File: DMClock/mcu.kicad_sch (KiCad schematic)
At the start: 0 parts

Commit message: adding mplabxide init files
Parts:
- added U1: PIC16F877A-I_P, Footprints:DIP254P1524X483-40, symbol PIC16F877A-I_P:PIC16F877A-I_P
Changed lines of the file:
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@@
 (kicad_sch (version 20230121) (generator eeschema)
   (paper "A4")
+  (symbol (lib_id "PIC16F877A-I_P:PIC16F877A-I_P") (at 136.652 90.678 0) (unit 1)
+    (in_bom yes) (on_board yes) (dnp no) (fields_autoplaced)
+    (property "Reference" "U1" (at 136.652 52.705 0)
+      (effects (font (size 1.27 1.27)))
+    )
+    (property "Value" "PIC16F877A-I_P" (at 136.652 55.245 0)
+      (effects (font (size 1.27 1.27)))
+    )
+    (property "Footprint" "Footprints:DIP254P1524X483-40" (at 136.652 90.678 0)
+      (effects (font (size 1.27 1.27)) (justify bottom) hide)
+    )
+    (property "Datasheet" "" (at 136.652 90.678 0)
+      (effects (font (size 1.27 1.27)) hide)
+    )
+    (property "MF" "Microchip" (at 136.652 90.678 0)
+      (effects (font (size 1.27 1.27)) (justify bottom) hide)
+    )
+    (property "Description" "\nMicrocontroller, 8bit PIC, 20MHz, 14.3kb, 256 B Flash, 40-Pin PDIP | Microchip Technology Inc. PIC16F877A-I/P\n" (at 136.652 90.678 0)
+      (effects (font (size 1.27 1.27)) (justify bottom) hide)
+    )
+    (property "PACKAGE" "DIP-40" (at 136.652 90.678 0)
+      (effects (font (size 1.27 1.27)) (justify bottom) hide)
+    )
+    (property "MPN" "PIC16F877A-I/P" (at 136.652 90.678 0)
+      (effects (font (size 1.27 1.27)) (justify bottom) hide)
+    )
+    (property "Price" "None" (at 136.652 90.678 0)
+      (effects (font (size 1.27 1.27)) (justify bottom) hide)
+    )
+    (property "Package" "DIP-40 Microchip" (at 136.652 90.678 0)
+      (effects (font (size 1.27 1.27)) (justify bottom) hide)
+    )
+    (property "OC_FARNELL" "9761446" (at 136.652 90.678 0)
+      (effects (font (size 1.27 1.27)) (justify bottom) hide)
+    )
+    (property "SnapEDA_Link" "https://www.snapeda.com/parts/PIC16F877A-I/P/Microchip/view-part/?ref=snap" (at 136.652 90.678 0)
+      (effects (font (size 1.27 1.27)) (justify bottom) hide)
+    )
+    (property "MP" "PIC16F877A-I/P" (at 136.652 90.678 0)
+      (effects (font (size 1.27 1.27)) (justify bottom) hide)
+    )
+    (property "SUPPLIER" "Microchip" (at 136.652 90.678 0)
+      (effects (font (size 1.27 1.27)) (justify bottom) hide)
+    )
+    (property "OC_NEWARK" "69K7640" (at 136.652 90.678 0)
+      (effects (font (size 1.27 1.27)) (justify bottom) hide)
+    )
+    (property "Availability" "In Stock" (at 136.652 90.678 0)
+      (effects (font (size 1.27 1.27)) (justify bottom) hide)
+    )
+    (property "Check_prices" "https://www.snapeda.com/parts/PIC16F877A-I/P/Microchip/view-part/?ref=eda" (at 136.652 90.678 0)
+      (effects (font (size 1.27 1.27)) (justify bottom) hide)
+    )
+    (pin "31")
+    (pin "20")
+    (pin "40")
+    (pin "5")
+    (pin "27")
+    (pin "33")
+    (pin "29")
+    (pin "14")
+    (pin "10")
+    (pin "28")
+    (pin "22")
+    (pin "21")
+    (pin "26")
+    (pin "3")
+    (pin "37")
+    (pin "12")
+    (pin "18")
+    (pin "1")
+    (pin "35")
+    (pin "39")
+    (pin "4")
+    (pin "6")
+    (pin "25")
+    (pin "38")
+    (pin "7")
+    (pin "19")
+    (pin "16")
+    (pin "8")
+    (pin "11")
+    (pin "32")
+    (pin "34")
+    (pin "15")
+    (pin "2")
+    (pin "24")
+    (pin "23")
+    (pin "36")
+    (pin "17")
+    (pin "9")
+    (pin "13")
+    (pin "30")
+    (instances
+      (project "DMClock"
+        (path "/b42b345f-a3f2-4eff-9109-2f4619119d33/8963f20e-1ea1-4ba0-ac82-90e49e093141"
+          (reference "U1") (unit 1)
+        )
+      )
+    )
+  )
 )

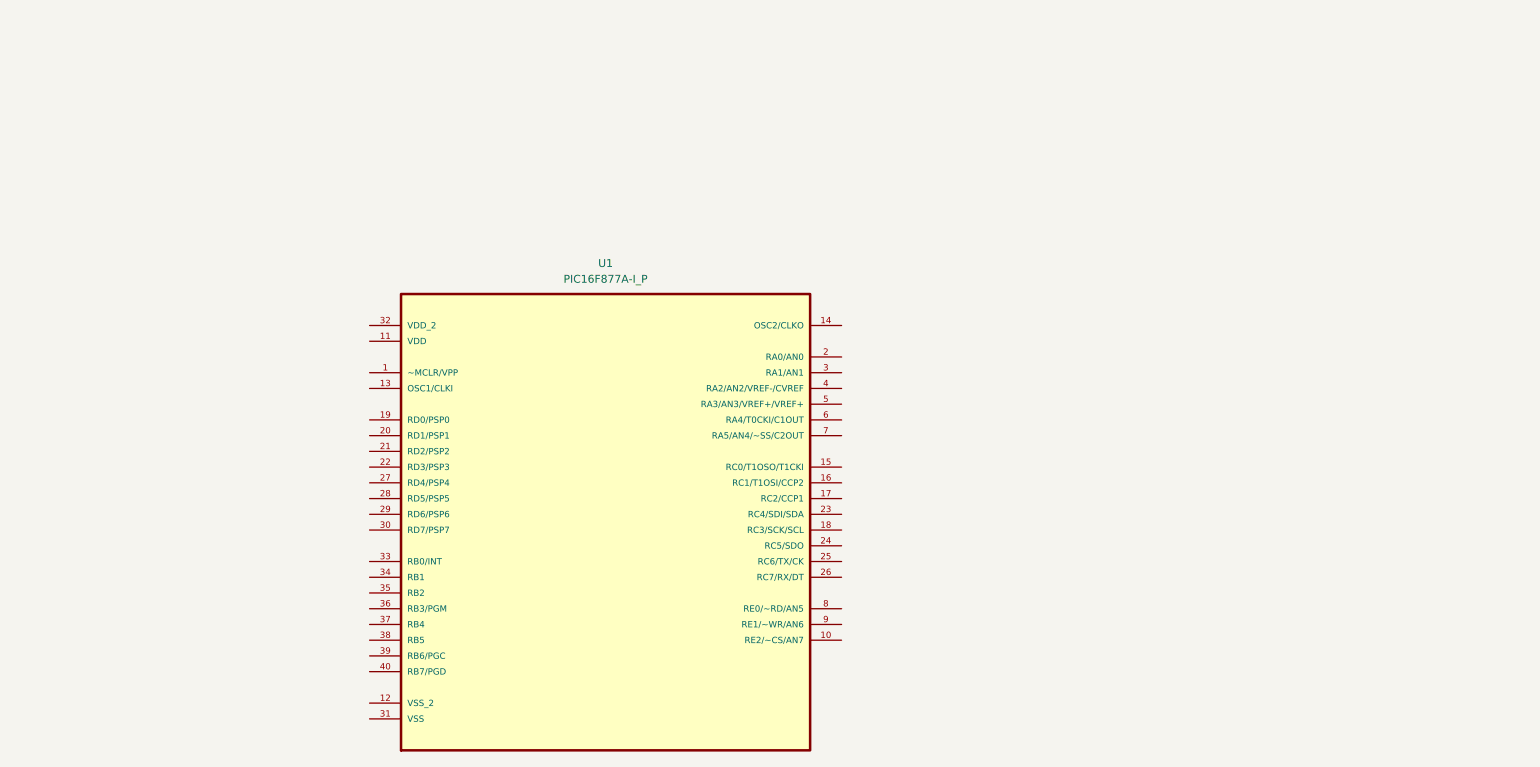
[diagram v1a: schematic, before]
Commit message: more modules added, still need to add a lot of footprints and see if there exist any sd card libraries for use with i2s
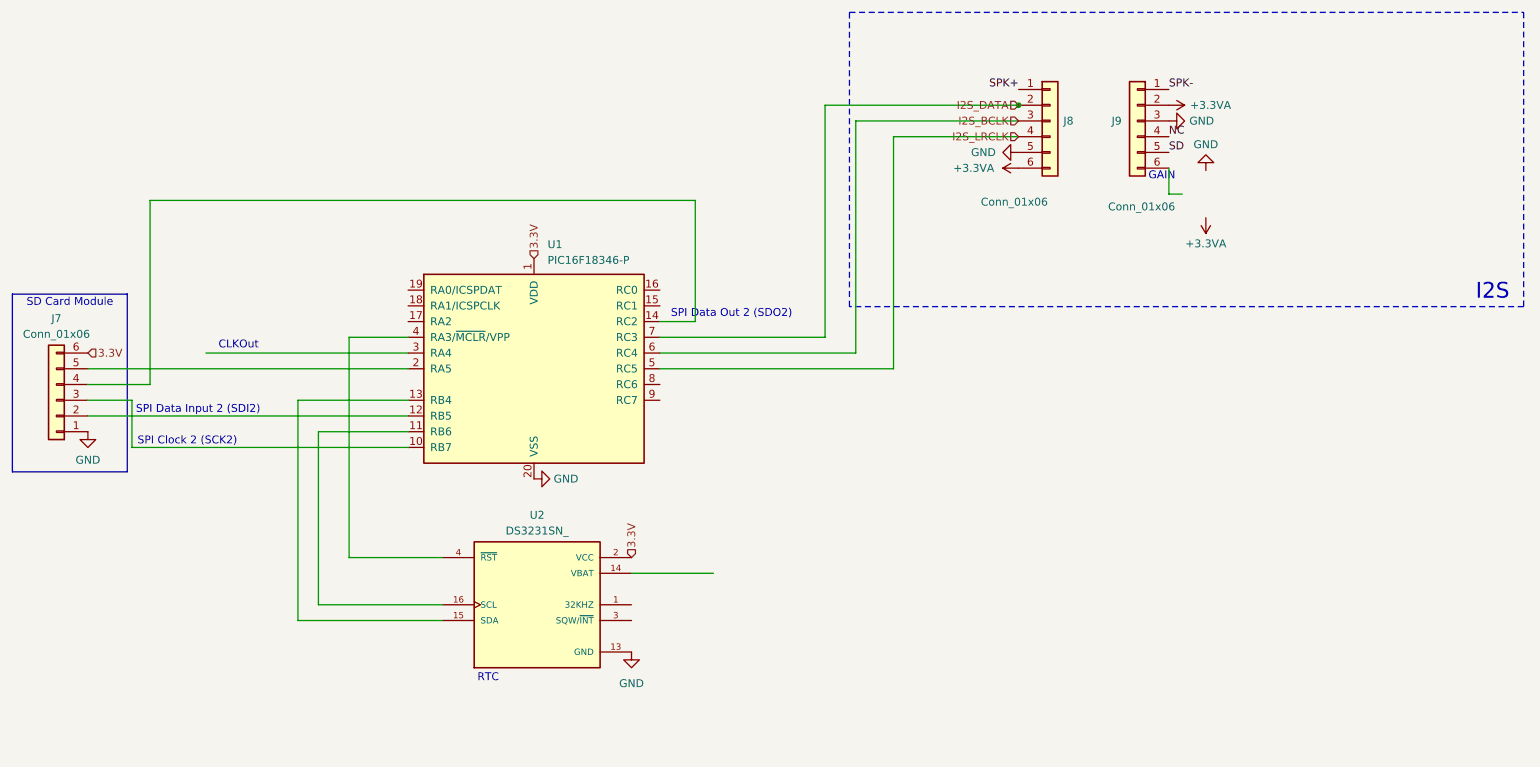
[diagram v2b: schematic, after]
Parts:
- removed U1: PIC16F877A-I_P, Footprints:DIP254P1524X483-40, symbol PIC16F877A-I_P:PIC16F877A-I_P
- added J7: Conn_01x06, symbol Connector_Generic:Conn_01x06
- added J8, J9: Conn_01x06, Connector_PinHeader_2.54mm:PinHeader_1x06_P2.54mm_Vertical, symbol Connector_Generic:Conn_01x06
- added U1: PIC16F18346-P, Package_DIP:DIP-20_W7.62mm, symbol MCU_Microchip_PIC16:PIC16F18346-P
- added U2: DS3231SN_, Footprints:SOIC127P1032X265-16N, symbol DS3231SN_:DS3231SN_
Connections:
- new net: U1.13 (RB4), U2.15 (SDA)
- new net: U1.11 (RB6), U2.16 (SCL)
- new net: U1.4 (RA3/~{MCLR}/VPP), U2.4 (~{RST})
- new net: J7.3 (Pin_3), U1.10 (RB7)
- new net: J7.2 (Pin_2), U1.12 (RB5)
- new net: J7.4 (Pin_4), U1.14 (RC2)
- new net: J7.5 (Pin_5), U1.2 (RA5)
- new net +3.3VA: J8.6 (Pin_6), J9.2 (Pin_2)
- new net 3.3V: J7.6 (Pin_6), U1.1 (VDD), U2.2 (VCC)
- new net GND: J7.1 (Pin_1), J8.5 (Pin_5), J9.3 (Pin_3), U1.20 (VSS), U2.13 (GND)
- new net I2S_BCLK: J8.3 (Pin_3), U1.6 (RC4)
- new net I2S_DATA: J8.2 (Pin_2), U1.7 (RC3)
- new net I2S_LRCLK: J8.4 (Pin_4), U1.5 (RC5)
- new net NC: J9.4 (Pin_4)
- new net SD: J9.5 (Pin_5)
- new net SPK+: J8.1 (Pin_1)
- new net SPK-: J9.1 (Pin_1)
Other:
- note added: "CLKOut"
- note added: "GAIN"
- note added: "I2S"
- note added: "RTC"
- note added: "SD Card Module"
- note added: "SPI Clock 2 (SCK2)"
- note added: "SPI Data Input 2 (SDI2)"
- note added: "SPI Data Out 2 (SDO2)"

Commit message: added more to schematic, hv622
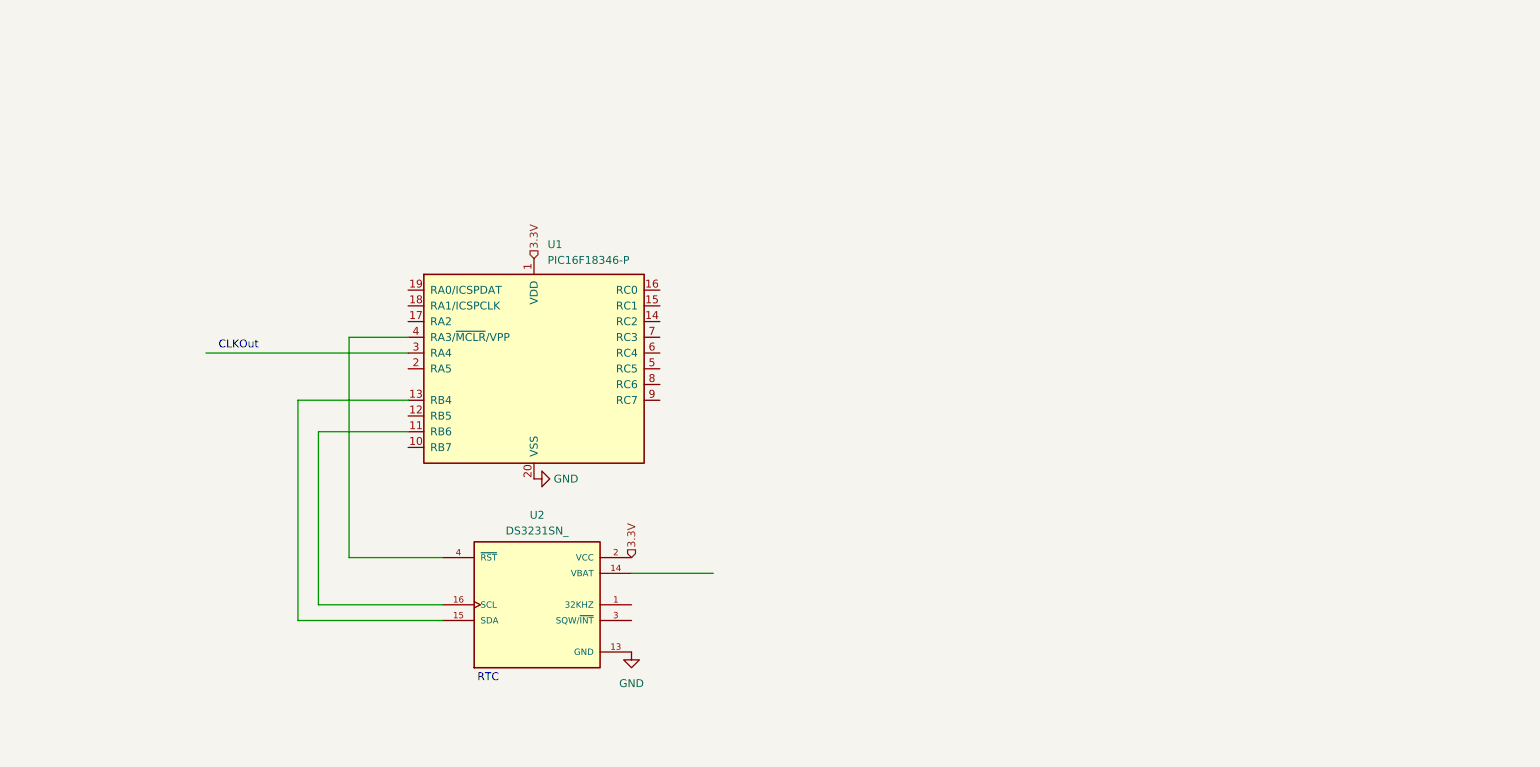
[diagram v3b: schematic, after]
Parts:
- removed J7: Conn_01x06, symbol Connector_Generic:Conn_01x06
- removed J8, J9: Conn_01x06, Connector_PinHeader_2.54mm:PinHeader_1x06_P2.54mm_Vertical, symbol Connector_Generic:Conn_01x06
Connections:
- net I2S_BCLK: no longer names the net of U1.6 (RC4)
- net I2S_DATA: no longer names the net of U1.7 (RC3)
- net I2S_LRCLK: no longer names the net of U1.5 (RC5)
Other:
- note removed: "GAIN"
- note removed: "I2S"
- note removed: "SD Card Module"
- note removed: "SPI Clock 2 (SCK2)"
- note removed: "SPI Data Input 2 (SDI2)"
- note removed: "SPI Data Out 2 (SDO2)"

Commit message: need to work on hvps logic converter
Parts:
- added BT1: 103, Footprints:BAT_103, symbol 103:103
- added R1, R2: 4.7K, Resistor_THT:R_Axial_DIN0204_L3.6mm_D1.6mm_P2.54mm_Vertical, symbol Device:R
- added SW1: SW_Push, symbol Switch:SW_Push
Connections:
- net 3.3V: now also R1.2, R2.2
- net GND: now also BT1.N, SW1.1
- net at U2.14 (VBAT): now also BT1.P
- net at U1.13 (RB4), U2.15 (SDA): now also R2.1
- net at U1.11 (RB6), U2.16 (SCL): now also R1.1
- net at U2.3 (SQW/~{INT}): now also U1.8 (RC6)
- net at U2.4 (~{RST}): now also SW1.2; no longer U1.4 (RA3/~{MCLR}/VPP)
- net CLK: now reaches U1.3 (RA4)
- net NOTLE: now reaches U1.5 (RC5)
- net NOTBL: now reaches U1.6 (RC4)
- net HV5622DataIn: now reaches U1.7 (RC3)
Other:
- note removed: "CLKOut"

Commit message: just need to finish pcb
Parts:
- added C10, C11: 0.1uF, Capacitor_SMD:C_0805_2012Metric, symbol Device:C
- added D2, D4: D, Diode_THT:D_A-405_P2.54mm_Vertical_AnodeUp, symbol Device:D
- added LS1, LS2: CPT-1255C-090, Footprints:CUI_CPT-1255C-090, symbol CPT-1255C-090:CPT-1255C-090
- added Q1, Q2: 2SC1815, Package_TO_SOT_THT:TO-92_Inline, symbol Transistor_BJT:2SC1815
- added R34, R35: 180, Resistor_THT:R_Axial_DIN0204_L3.6mm_D1.6mm_P2.54mm_Vertical, symbol Device:R
- added SW10, SW7, SW8, SW9: SW_Push, Connector_PinHeader_2.54mm:PinHeader_1x02_P2.54mm_Vertical, symbol Switch:SW_Push
- added SW3: SW_SP3T (mode select), Footprints:OS102011MS8QP1, symbol Switch:SW_SP3T
- SW1: footprint (none) -> Connector_PinHeader_2.54mm:PinHeader_1x02_P2.54mm_Vertical
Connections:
- net 3.3V: now also C11.1, D2.1 (K), D4.1 (K), LS1.P, LS2.P, SW10.2, SW3.3, SW7.1, SW8.2, SW9.1; no longer U2.2 (VCC)
- net GND: now also C10.2, C11.2, Q1.1 (E), Q2.1 (E)
- net HV5622DataIn: now also U1.16 (RC0); no longer U1.7 (RC3)
- net NOTBL: now also U1.15 (RC1); no longer U1.6 (RC4)
- net NOTLE: now also U1.14 (RC2); no longer U1.5 (RC5)
- net at U2.3 (SQW/~{INT}): now also U1.9 (RC7); no longer U1.8 (RC6)
- net at U1.10 (RB7): now also SW8.1
- net at U1.12 (RB5): now also SW7.2
- net at U1.17 (RA2): now also SW3.4
- net at U1.18 (RA1/ICSPCLK): now also SW3.2
- net at U1.19 (RA0/ICSPDAT): now also SW3.1
- new net: D2.2 (A), LS2.N, Q2.2 (C)
- new net: SW10.1, U1.6 (RC4)
- new net: C10.1, U2.2 (VCC)
- new net: Q2.3 (B), R35.1
- new net: D4.2 (A), LS1.N, Q1.2 (C)
- new net: Q1.3 (B), R34.2
- new net: R35.2, U1.5 (RC5)
- new net: SW9.2, U1.8 (RC6)
- new net: R34.1, U1.7 (RC3)
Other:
- note added: "CCP1_PWM1"
- note added: "CCP2_PWM2"
- note added: "Clock Mode (Alarm Off)"
- note added: "Clock Mode (Alarm On)"
- note added: "DM Mode"

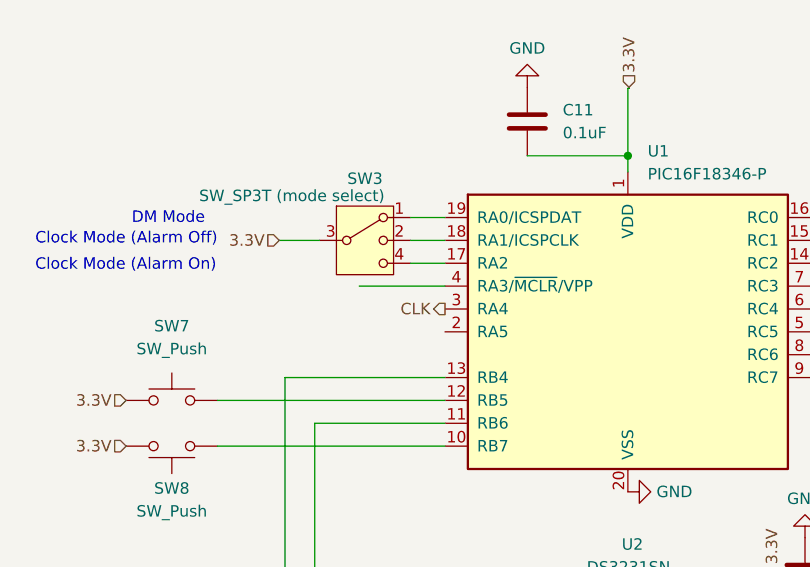
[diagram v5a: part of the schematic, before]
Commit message: finished second layer. need to finalize both first and second (double checking everything looks right, double check pwm pins, add ground plane, and finally send to pcbway. im kinda slow but hopefully done with first version pcb by tomorrow.
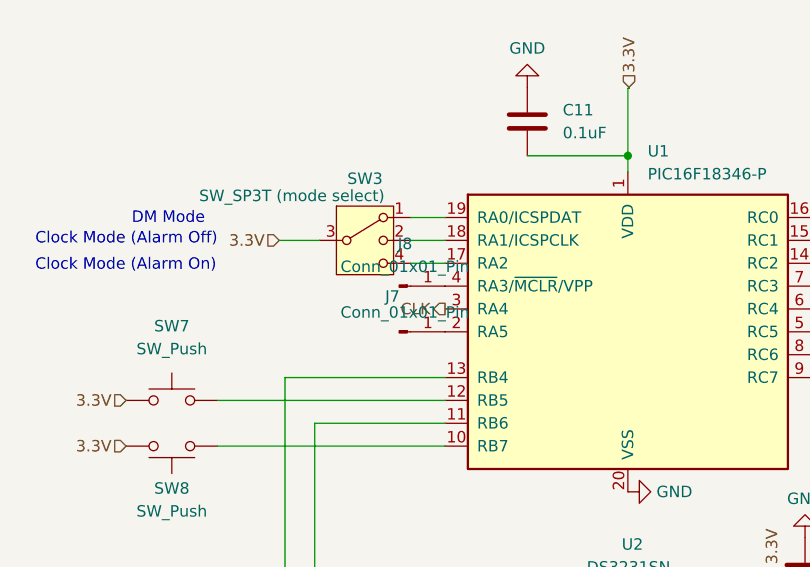
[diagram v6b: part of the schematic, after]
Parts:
- added J7, J8: Conn_01x01_Pin, Connector_PinSocket_2.54mm:PinSocket_1x01_P2.54mm_Vertical, symbol Connector:Conn_01x01_Pin
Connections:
- net at U1.2 (RA5): now also J7.1 (Pin_1)
- net at U1.4 (RA3/~{MCLR}/VPP): now also J8.1 (Pin_1)
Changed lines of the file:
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@@
-    (stroke (width 0) (type default))
-  )
-  (wire (pts (xy 95.25 64.643) (xy 104.775 64.643))
     (stroke (width 0) (type default))
   )
@@
     )
   )
+  (symbol (lib_id "Connector:Conn_01x01_Pin") (at 99.695 69.723 0) (unit 1)
+    (in_bom yes) (on_board yes) (dnp no)
+    (property "Reference" "J7" (at 98.933 65.786 0)
+      (effects (font (size 1.27 1.27)))
+    )
+    (property "Value" "Conn_01x01_Pin" (at 100.33 67.564 0)
+      (effects (font (size 1.27 1.27)))
+    )
+    (property "Footprint" "Connector_PinSocket_2.54mm:PinSocket_1x01_P2.54mm_Vertical" (at 99.695 69.723 0)
+      (effects (font (size 1.27 1.27)) hide)
+    )
+    (property "Datasheet" "~" (at 99.695 69.723 0)
+      (effects (font (size 1.27 1.27)) hide)
+    )
+    (pin "1")
+    (instances
+      (project "DMClock"
+        (path "/b42b345f-a3f2-4eff-9109-2f4619119d33/8963f20e-1ea1-4ba0-ac82-90e49e093141"
+          (reference "J7") (unit 1)
+        )
+      )
+    )
+  )
   (symbol (lib_id "Switch:SW_Push") (at 123.825 128.905 180) (unit 1)
     (in_bom yes) (on_board yes) (dnp no) (fields_autoplaced)
@@
         )
       )
+    )
+  )
+  (symbol (lib_id "Connector:Conn_01x01_Pin") (at 99.695 64.643 0) (unit 1)
+    (in_bom yes) (on_board yes) (dnp no) (fields_autoplaced)
+    (property "Reference" "J8" (at 100.33 59.944 0)
+      (effects (font (size 1.27 1.27)))
+    )
+    (property "Value" "Conn_01x01_Pin" (at 100.33 62.484 0)
+      (effects (font (size 1.27 1.27)))
+    )
+    (property "Footprint" "Connector_PinSocket_2.54mm:PinSocket_1x01_P2.54mm_Vertical" (at 99.695 64.643 0)
+      (effects (font (size 1.27 1.27)) hide)
+    )
+    (property "Datasheet" "~" (at 99.695 64.643 0)
+      (effects (font (size 1.27 1.27)) hide)
+    )
+    (pin "1")
+    (instances
+      (project "DMClock"
+        (path "/b42b345f-a3f2-4eff-9109-2f4619119d33/8963f20e-1ea1-4ba0-ac82-90e49e093141"
+          (reference "J8") (unit 1)
+        )
+      )

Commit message: finished v.1
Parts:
- removed J7, J8: Conn_01x01_Pin, Connector_PinSocket_2.54mm:PinSocket_1x01_P2.54mm_Vertical, symbol Connector:Conn_01x01_Pin
- added J7, J9: Conn_01x02_Pin, Connector_PinSocket_2.54mm:PinSocket_1x02_P2.54mm_Vertical, symbol Connector:Conn_01x02_Pin
- added R3, R36, R37, R38, R39, R40, R41, R42: 4.7K, Resistor_THT:R_Axial_DIN0204_L3.6mm_D1.6mm_P2.54mm_Vertical, symbol Device:R
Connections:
- net 3.3V: now also C10.1, U2.2 (VCC), R42.2
- net GND: now also U2.10 (N.C.), U2.11 (N.C.), U2.12 (N.C.), U2.5 (N.C.), U2.6 (N.C.), U2.7 (N.C.), U2.8 (N.C.), U2.9 (N.C.), J7.2 (Pin_2), J9.2 (Pin_2), R3.2, R36.2, R37.2, R38.2, R39.2, R40.2, R41.2
- net at SW10.1, U1.6 (RC4): now also R38.1
- net at U1.9 (RC7), U2.3 (SQW/~{INT}): now also R42.1
- net at SW8.1, U1.10 (RB7): now also R3.1
- net at U1.2 (RA5): now also J9.1 (Pin_1)
- net at U1.4 (RA3/~{MCLR}/VPP): now also J7.1 (Pin_1)
- net at SW9.2, U1.8 (RC6): now also R37.1
- net at SW7.2, U1.12 (RB5): now also R36.1
- net at SW3.4, U1.17 (RA2): now also R41.1
- net at SW3.2, U1.18 (RA1/ICSPCLK): now also R40.1
- net at SW3.1, U1.19 (RA0/ICSPDAT): now also R39.1

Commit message: initial mpe files
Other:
- note added: "PWM5"
- note added: "PWM6"
- note removed: "CCP1_PWM1"
- note removed: "CCP2_PWM2"
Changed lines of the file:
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@@
     (effects (font (size 1.27 1.27)) (justify right bottom))
   )
-  (text "CCP2_PWM2" (at 155.702 64.135 0)
+  (text "PWM6" (at 155.702 64.135 0)
     (effects (font (size 1.27 1.27)) (justify left bottom))
   )
-  (text "CCP1_PWM1" (at 155.829 69.977 0)
+  (text "PWM5" (at 155.829 69.977 0)
     (effects (font (size 1.27 1.27)) (justify left bottom))
   )
